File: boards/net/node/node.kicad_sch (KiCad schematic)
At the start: 0 parts

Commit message: net/node: RP2040 sensor-net node schematic with pogo programming pads and sensor variants
Proof-of-concept cell for a tiled sensor net: RP2040, W25Q16, 12 MHz crystal, ME6211 LDO,
four JST-XH neighbour links (5 V, single-wire open-drain UART, GND), WS2812B-2020 LED behind
a diode drop, buzzer driver, and a sensor port. No USB connector: J6 is a 2x4 pogo pad array
carrying SWD, USB D+/D-, RUN, BOOT and 5 V. Sensor options are KiCad 10 design variants in
one schematic: default VL53L0X ToF, "vib" SW-18010P spring switch, "bare" header only.
Schematic generated by generate/schematic.py; ERC clean; PCB not laid out yet.

schgen: local net labels, dnp, in_pos_files, per-variant overrides, prop_rot.
lib: SW-18010P vibration switch footprint.
CLAUDE.md: variant file syntax, label/property text notes, per-variant jobset idea.

Co-Authored-By: Claude Fable 5.1 <noreply@anthropic.com>
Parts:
- added BZ1: Buzzer 5V, Buzzer_Beeper:Buzzer_12x9.5RM7.6, symbol Device:Buzzer
- added C1, C2: 27p, Capacitor_SMD:C_0603_1608Metric, symbol Device:C
- added C10, C14, C15, C16, C19, C20, C22, C3, C4, C5, C6, C7, C8, C9: 100n, Capacitor_SMD:C_0603_1608Metric, symbol Device:C
- added C11, C13: 1u, Capacitor_SMD:C_0603_1608Metric, symbol Device:C
- added C12, C17, C18: 10u, Capacitor_SMD:C_0603_1608Metric, symbol Device:C
- added C21: 4u7, Capacitor_SMD:C_0603_1608Metric, symbol Device:C
- added D1, D3: 1N4148W, Diode_SMD:D_SOD-123, symbol Device:D
- added D2: WS2812B-2020, LED_SMD:LED_WS2812B-2020_PLCC4_2.0x2.0mm, symbol LED:WS2812B-2020
- added H1, H2, H3, H4: M2, MountingHole:MountingHole_2.2mm_M2, symbol Mechanical:MountingHole
- added J1: N, Connector_JST:JST_XH_B3B-XH-A_1x03_P2.50mm_Vertical, symbol Connector_Generic:Conn_01x03
- added J2: E, Connector_JST:JST_XH_B3B-XH-A_1x03_P2.50mm_Vertical, symbol Connector_Generic:Conn_01x03
- added J3: S, Connector_JST:JST_XH_B3B-XH-A_1x03_P2.50mm_Vertical, symbol Connector_Generic:Conn_01x03
- added J4: W, Connector_JST:JST_XH_B3B-XH-A_1x03_P2.50mm_Vertical, symbol Connector_Generic:Conn_01x03
- added J5: SENSOR, Connector_PinHeader_2.54mm:PinHeader_1x07_P2.54mm_Vertical, symbol Connector_Generic:Conn_01x07
- added J6: PROG, Connector_PinHeader_2.54mm:PinHeader_2x04_P2.54mm_Vertical_SMD, symbol Connector_Generic:Conn_02x04_Odd_Even
- added Q1: 2N7002, Package_TO_SOT_SMD:SOT-23, symbol Transistor_FET:2N7002
- added R1, R17: 1k, Resistor_SMD:R_0603_1608Metric, symbol Device:R
- added R10, R12, R14, R4, R5, R8: 4k7, Resistor_SMD:R_0603_1608Metric, symbol Device:R
- added R11, R13, R7, R9: 100, Resistor_SMD:R_0603_1608Metric, symbol Device:R
- added R15, R16: 27, Resistor_SMD:R_0603_1608Metric, symbol Device:R
- added R18: 100k, Resistor_SMD:R_0603_1608Metric, symbol Device:R
- added R2, R3, R6: 10k, Resistor_SMD:R_0603_1608Metric, symbol Device:R
- added SW1: SW-18010P, boards:SW-18010P, symbol Switch:SW_SPST
- added U1: RP2040, Package_DFN_QFN:QFN-56-1EP_7x7mm_P0.4mm_EP3.2x3.2mm, symbol MCU_RaspberryPi:RP2040
- added U2: W25Q16JVSSIQ, Package_SO:SOIC-8_5.3x5.3mm_P1.27mm, symbol Memory_Flash:W25Q16JVSS
- added U3: VL53L0CXV0DH/1, OptoDevice:ST_VL53L0X, symbol Sensor_Distance:VL53L0CXV0DH1
- added U4: ME6211C33M5G, Package_TO_SOT_SMD:SOT-23-5, symbol Regulator_Linear:ME6211C33M5
- added Y1: 12MHz, Crystal:Crystal_SMD_3225-4Pin_3.2x2.5mm, symbol Device:Crystal_GND24
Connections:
- new net: C2.2, R1.1, Y1.3
- new net: R1.2, U1.21 (XOUT)
- new net: J3.2 (Pin_2), R11.2
- new net: Q1.1 (G), R17.2, R18.1
- new net: BZ1.2 (-), D3.2 (A), Q1.3 (D)
- new net: C1.2, U1.20 (XIN), Y1.1
- new net: J1.2 (Pin_2), R7.2
- new net: J2.2 (Pin_2), R9.2
- new net: J6.1 (Pin_1), R15.1
- new net: J4.2 (Pin_2), R13.2
- new net: J6.3 (Pin_3), R16.1
- new net +3V3: C10.1, C11.1, C12.1, C16.1, C18.1, C20.1, C21.1, C3.1, C4.1, C5.1, C6.1, C7.1, C8.1, C9.1, J5.2 (Pin_2), R10.1, R12.1, R14.1, R2.1, R3.1, R4.1, R5.1, R6.1, R8.1, U1.1 (IOVDD), U1.10 (IOVDD), U1.22 (IOVDD), U1.33 (IOVDD), U1.42 (IOVDD), U1.43 (ADC_AVDD), U1.44 (VREG_VIN), U1.48 (USB_VDD), U1.49 (IOVDD), U2.8 (VCC), U3.1 (AVDDVCSEL), U3.11 (AVDD), U4.5 (V_{OUT})
- new net +5V: BZ1.1 (+), C17.1, D1.2 (A), D3.1 (K), J1.1 (Pin_1), J2.1 (Pin_1), J3.1 (Pin_1), J4.1 (Pin_1), J5.1 (Pin_1), J6.7 (Pin_7), U4.1 (V_{IN}), U4.3 (CE)
- new net BUZZ: R17.1, U1.7 (GPIO5)
- new net DVDD: C13.1, C14.1, C15.1, U1.23 (DVDD), U1.45 (VREG_VOUT), U1.50 (DVDD)
- new net GND: C1.1, C10.2, C11.2, C12.2, C13.2, C14.2, C15.2, C16.2, C17.2, C18.2, C19.2, C2.1, C20.2, C21.2, C22.2, C3.2, C4.2, C5.2, C6.2, C7.2, C8.2, C9.2, D2.2 (VSS), J1.3 (Pin_3), J2.3 (Pin_3), J3.3 (Pin_3), J4.3 (Pin_3), J5.7 (Pin_7), J6.5 (Pin_5), Q1.2 (S), R18.2, SW1.1 (A), U1.19 (TESTEN), U1.57 (GND), U2.4 (GND), U3.12 (GND), U3.2 (AVSSVCSEL), U3.3 (GND), U3.4 (GND), U3.6 (GND), U4.2 (V_{SS}), Y1.2 (G), Y1.4 (G)
- new net LED_DIN: D2.3 (DIN), U1.6 (GPIO4)
- new net LED_VDD: C19.1, D1.1 (K), D2.4 (VDD)
- new net LINK_E: R10.2, R9.1, U1.3 (GPIO1)
- new net LINK_N: R7.1, R8.2, U1.2 (GPIO0)
- new net LINK_S: R11.1, R12.2, U1.4 (GPIO2)
- new net LINK_W: R13.1, R14.2, U1.5 (GPIO3)
- new net QSPI_SCLK: U1.52 (QSPI_SCLK), U2.6 (CLK)
- new net QSPI_SD0: U1.53 (QSPI_SD0), U2.5 (DI/IO_{0})
- new net QSPI_SD1: U1.55 (QSPI_SD1), U2.2 (DO/IO_{1})
- new net QSPI_SD2: U1.54 (QSPI_SD2), U2.3 (~{WP}/IO_{2})
- new net QSPI_SD3: U1.51 (QSPI_SD3), U2.7 (~{HOLD}/~{RESET}/IO_{3})
- new net QSPI_SS: J6.8 (Pin_8), R3.2, U1.56 (~{QSPI_SS}), U2.1 (~{CS})
- new net RUN: J6.6 (Pin_6), R2.2, U1.26 (RUN)
- new net SCL: J5.5 (Pin_5), R5.2, U1.12 (GPIO9), U3.10 (SCL)
- new net SDA: J5.4 (Pin_4), R4.2, U1.11 (GPIO8), U3.9 (SDA)
- new net SENS_AIN: J5.6 (Pin_6), U1.38 (GPIO26/ADC0)
- new net SENS_INT: C22.1, J5.3 (Pin_3), R6.2, SW1.2 (B), U1.8 (GPIO6), U3.7 (GPIO1)
- new net SENS_XSHUT: U1.9 (GPIO7), U3.5 (XSHUT)
- new net SWCLK: J6.4 (Pin_4), U1.24 (SWCLK)
- new net SWDIO: J6.2 (Pin_2), U1.25 (SWDIO)
- new net USB_DM: R16.2, U1.46 (USB_DM)
- new net USB_DP: R15.2, U1.47 (USB_DP)
- no-connect marks 0 -> 22
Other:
- note added: "5 V comes in over the link connectors; any node can also be fed from the programming jig."
- note added: "D1 drops the LED supply to ~4.3 V so 3.3 V logic meets the WS2812B VIH (0.7 VDD)."
- note added: "J6: 2x4 pogo pads (2.54 mm), nothing fitted. SWD, or USB via 27R with BOOT grounding QSPI_SS."
- note added: "Neighbour links: 5 V, single-wire half-duplex UART (open drain, 4k7 pull-up), GND. Straight 3-wire cable, no crossover."
- note added: "Pull-ups: RUN, QSPI_SS (boot), I2C, sensor INT (open-drain GPIO1 / switch)."
- note added: "RP2040 decoupling: one 100 nF per IOVDD pin (6), USB_VDD, ADC_AVDD; 1 uF on VREG_VIN; 10 uF bulk. DVDD: 1 uF + 2 x 100 nF."
- note added: "Sensor port. J5 takes off-board modules (LD2410, AM312 PIR, I2C breakouts). U3 = default variant, SW1 = "vib" variant, "bare" = header only."
- note added: "debounce"
- title: node -> Net node: RP2040, 4 neighbour links, RGB LED, buzzer, sensor port

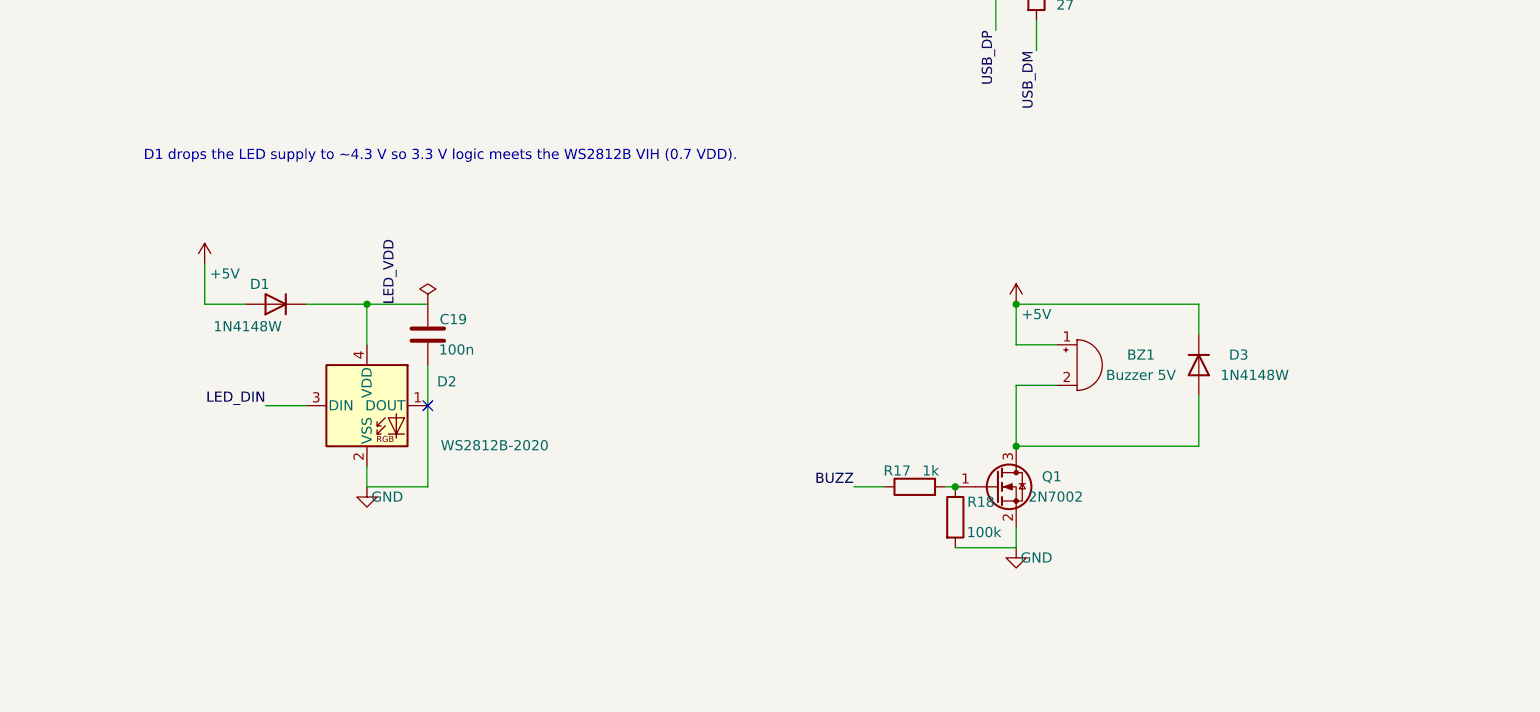
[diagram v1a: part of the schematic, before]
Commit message: net/node: second WS2812B-2020 (D4, DNP) chained on D2 for a brighter node
Regenerated schematic; C19 moved to the rail end, buzzer block shifted right.
ERC/DRC clean, D4 excluded from all three variant BOMs.

Co-Authored-By: Claude Fable 5.1 <noreply@anthropic.com>
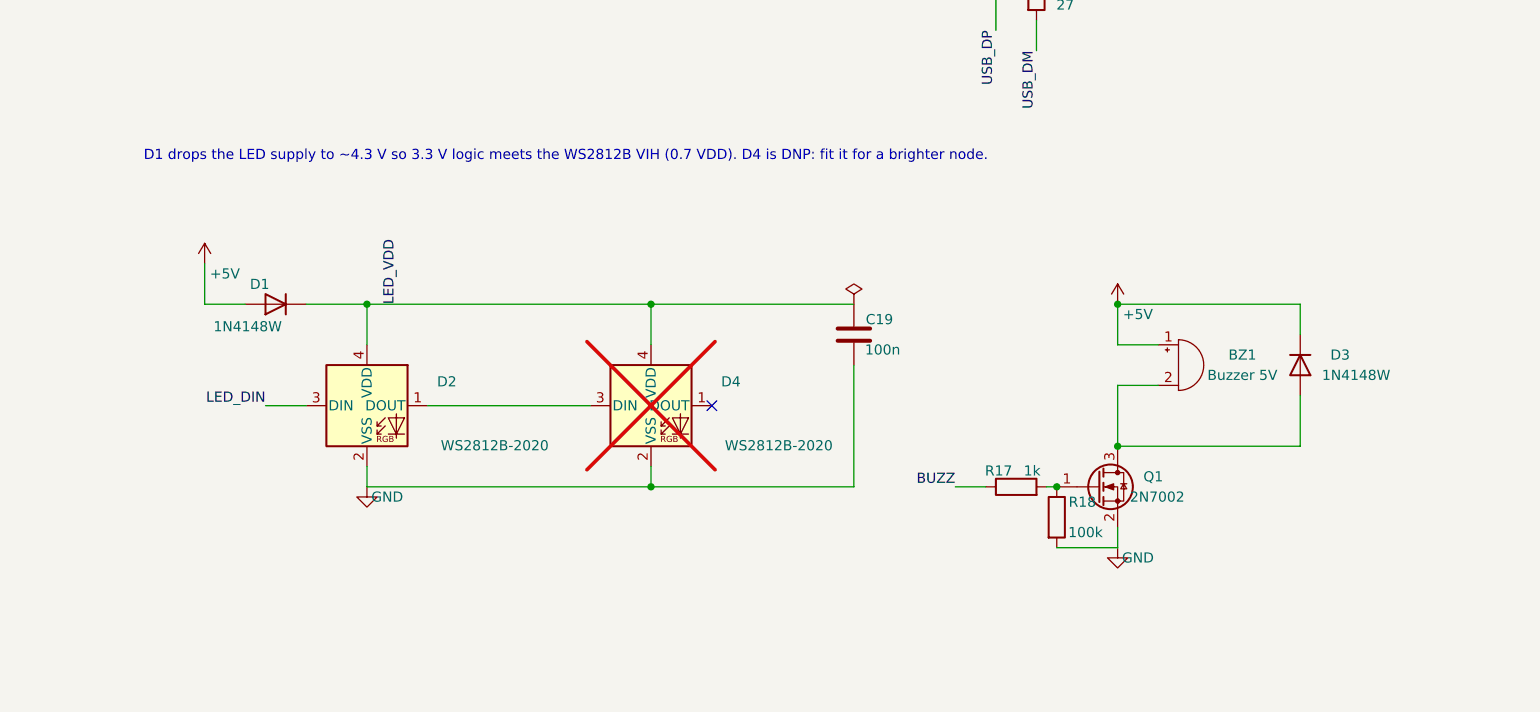
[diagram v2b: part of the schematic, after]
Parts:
- added D4: WS2812B-2020, LED_SMD:LED_WS2812B-2020_PLCC4_2.0x2.0mm, symbol LED:WS2812B-2020
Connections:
- net GND: now also D4.2 (VSS)
- net LED_VDD: now also D4.4 (VDD)
- net at D2.1 (DOUT): now also D4.3 (DIN)
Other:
- note added: "D1 drops the LED supply to ~4.3 V so 3.3 V logic meets the WS2812B VIH (0.7 VDD). D4 is DNP: fit it for a brighter node."
- note removed: "D1 drops the LED supply to ~4.3 V so 3.3 V logic meets the WS2812B VIH (0.7 VDD)."

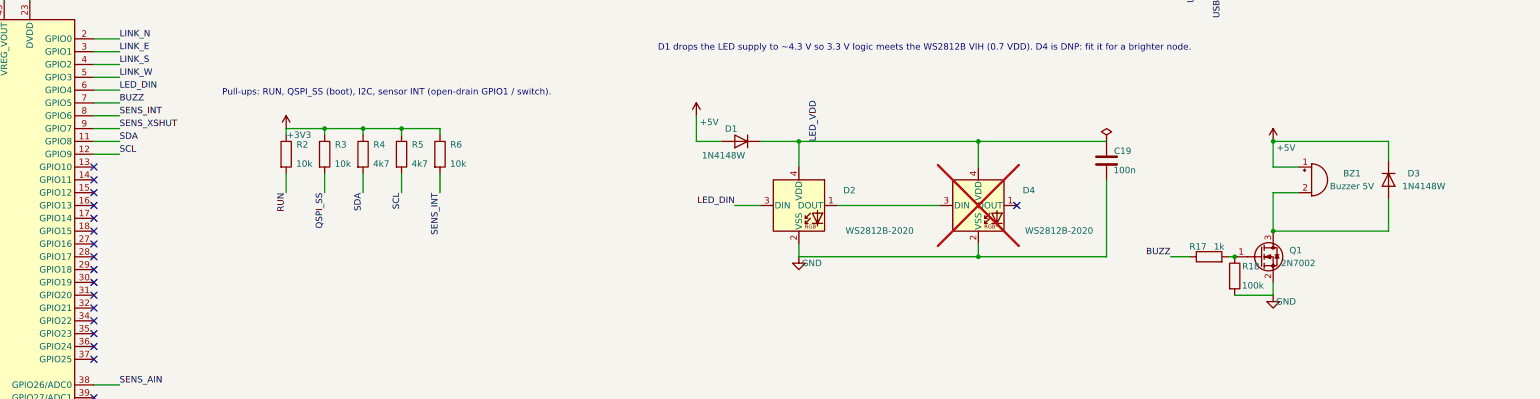
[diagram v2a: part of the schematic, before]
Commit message: net/node: drop the buzzer; pcbgen: idempotent inner layers, attr-less footprints keep flags, board-side variants
- pcbgen: InN.Cu layers are rebuilt from scratch (a generator reading its own output
  no longer accumulates copies); footprints without an attr clause still get dnp /
  exclude flags; per-variant dnp/exclude overrides from the netlist are written as
  KiCad 10 (variants ...) on the board and (variant ...) on each footprint, so
  `pcb export pos --variant` now agrees with the BOM. Tests cover all three.
- net/node: BZ1/Q1/R17/R18/D3 removed (largest part after the connectors, and a 5 V
  budget problem next to the LEDs); GPIO5 is a no-connect. ERC clean. README: buzzer
  decision, jig row spacing (5.05 mm), D4 two-pixel note, LCSC list.

Co-Authored-By: Claude Fable 5.1 <noreply@anthropic.com>
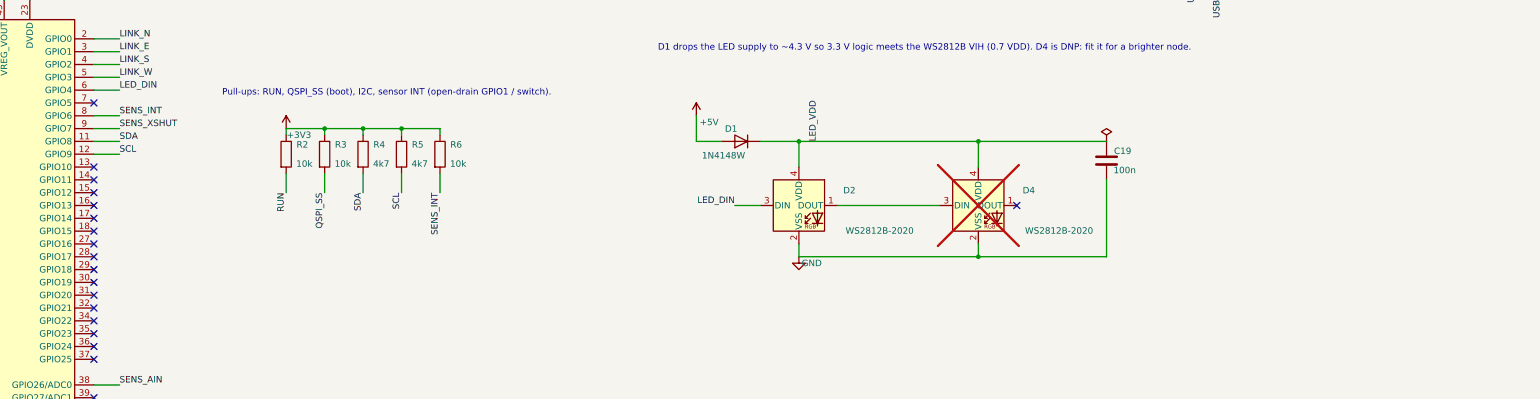
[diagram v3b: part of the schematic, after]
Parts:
- removed BZ1: Buzzer 5V, Buzzer_Beeper:Buzzer_12x9.5RM7.6, symbol Device:Buzzer
- removed D3: 1N4148W, Diode_SMD:D_SOD-123, symbol Device:D
- removed Q1: 2N7002, Package_TO_SOT_SMD:SOT-23, symbol Transistor_FET:2N7002
- removed R17: 1k, Resistor_SMD:R_0603_1608Metric, symbol Device:R
- removed R18: 100k, Resistor_SMD:R_0603_1608Metric, symbol Device:R
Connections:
- net BUZZ: no longer names the net of U1.7 (GPIO5)
- no-connect marks 22 -> 23
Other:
- title: Net node: RP2040, 4 neighbour links, RGB LED, buzzer, sensor port -> Net node: RP2040, 4 neighbour links, RGB LED, sensor port

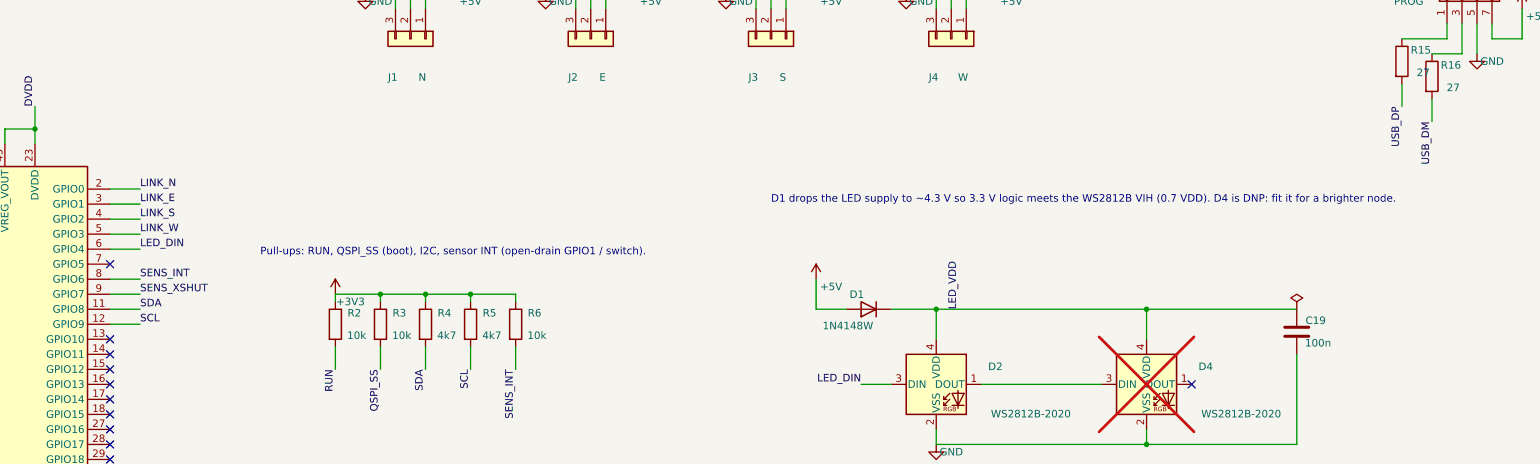
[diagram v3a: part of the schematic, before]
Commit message: net/node: place and route the board (DRC clean); pcbgen: solid_pads, zone thermals, empty fields
- Sensor GPIOs moved: XSHUT GPIO7->GPIO5, SDA/SCL GPIO8/9 -> GPIO10/11 (I2C1) so IOVDD
  pin 10's neighbours stay unrouted and it can via to the plane; J6 USB pins swapped
  (1 = DM, 3 = DP) so the traces do not cross. Schematic regenerated, ERC clean.
- pcb.py: U1 at (14, 13), 4 layers, every net routed: up-left SWD/crystal fan onto
  1.2 mm rows, down-right GPIO fan onto 0.7 mm columns, QSPI around the flash, west
  B.Cu lanes ending in vias inside the pogo pads, 0.8 mm 5 V ring notched around three
  M2 keepouts and open at the top-left corner, planes on In1/In2. make check: 0
  violations, 0 unconnected, 0 parity issues (two dangling-end warnings = the open ring).
- pcbgen: solid_pads= (J4 pin 3), zone thermal_gap/thermal_bridge, empty schematic fields
  written as empty properties (parity), ref_pos documented as rotating with the part.
- READMEs: PCB section rewritten for the routed board, resume path, generate commands.
  CLAUDE.md: 0.4 mm pitch escape/via rules, pad offsets, flatpak KiCad setup.

Co-Authored-By: Claude Fable 5.1 <noreply@anthropic.com>
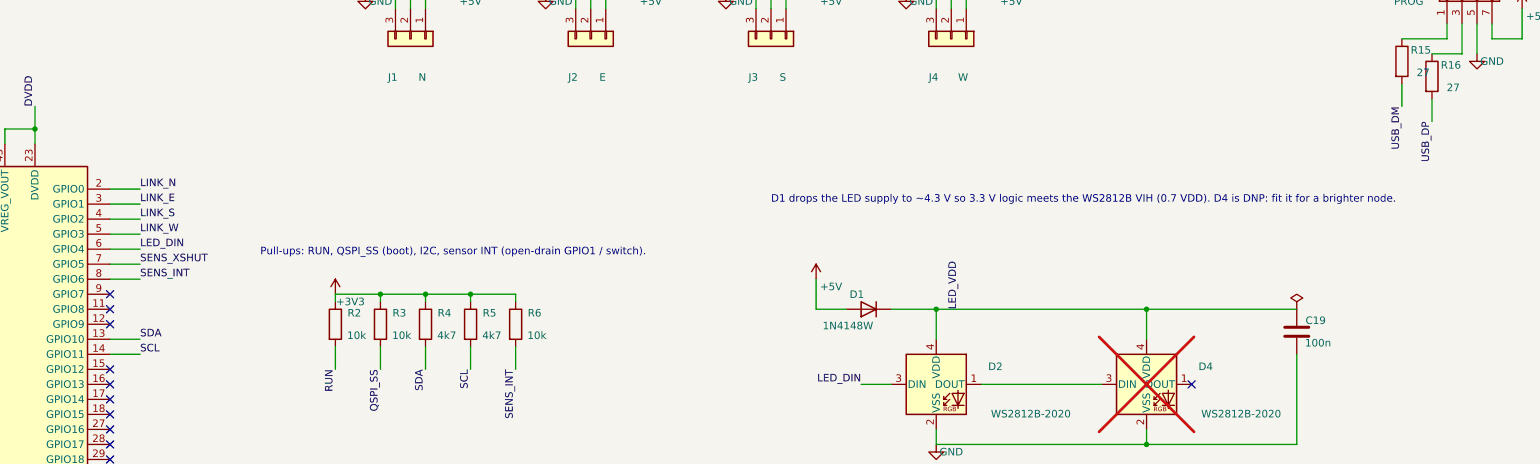
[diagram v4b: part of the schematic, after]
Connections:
- net SCL: now also U1.14 (GPIO11); no longer U1.12 (GPIO9)
- net SDA: now also U1.13 (GPIO10); no longer U1.11 (GPIO8)
- net SENS_XSHUT: now also U1.7 (GPIO5); no longer U1.9 (GPIO7)
- net USB_DM: now also R15.2; no longer R16.2
- net USB_DP: now also R16.2; no longer R15.2
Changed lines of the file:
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@@
 	(wire
 		(pts
-			(xy 139.7 104.14)
-			(xy 144.78 104.14)
+			(xy 139.7 101.6)
+			(xy 144.78 101.6)
 		)
 		(stroke
@@
 		)
 	)
-	(label "SENS_INT"
-		(at 144.78 104.14 0)
+	(label "SENS_XSHUT"
+		(at 144.78 101.6 0)
 		(effects
 			(font
@@
 	(wire
 		(pts
-			(xy 139.7 106.68)
-			(xy 144.78 106.68)
+			(xy 139.7 104.14)
+			(xy 144.78 104.14)
 		)
 		(stroke
@@
 		)
 	)
-	(label "SENS_XSHUT"
-		(at 144.78 106.68 0)
+	(label "SENS_INT"
+		(at 144.78 104.14 0)
 		(effects
 			(font
@@
 	(wire
 		(pts
-			(xy 139.7 109.22)
-			(xy 144.78 109.22)
+			(xy 139.7 114.3)
+			(xy 144.78 114.3)
 		)
 		(stroke
@@
 	)
 	(label "SDA"
-		(at 144.78 109.22 0)
+		(at 144.78 114.3 0)
 		(effects
 			(font
@@
 	(wire
 		(pts
-			(xy 139.7 111.76)
-			(xy 144.78 111.76)
+			(xy 139.7 116.84)
+			(xy 144.78 116.84)
 		)
 		(stroke
@@
 	)
 	(label "SCL"
-		(at 144.78 111.76 0)
+		(at 144.78 116.84 0)
 		(effects
 			(font
@@
 	)
 	(no_connect
-		(at 139.7 101.6)
+		(at 139.7 106.68)
 	)
 	(no_connect
-		(at 139.7 114.3)
+		(at 139.7 109.22)
 	)
 	(no_connect
-		(at 139.7 116.84)
+		(at 139.7 111.76)
 	)
 	(no_connect
@@
 		)
 	)
-	(label "USB_DP"
+	(label "USB_DM"
 		(at 358.14 74.93 270)
 		(effects
@@
 		)
 	)
-	(label "USB_DM"
+	(label "USB_DP"
 		(at 363.22 77.47 270)
 		(effects

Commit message: net/node: piezo sounder BZ1 (Murata PKMCS0909E, 9 mm SMD) on GPIO12/13 via 100 R, antiphase drive
Schematic only: BZ1 + R17/R18, ERC clean, netlist regenerated; placement and routing follow.
README: decision, GPIO map, refdes table.

Co-Authored-By: Claude Fable 5.1 <noreply@anthropic.com>
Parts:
- added BZ1: PKMCS0909E4000-R1, Buzzer_Beeper:Buzzer_Murata_PKMCS0909E, symbol Device:Buzzer
- added R17, R18: 100, Resistor_SMD:R_0603_1608Metric, symbol Device:R
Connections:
- net BUZZ_A: now reaches U1.15 (GPIO12)
- net BUZZ_A: now also R17.1
- net BUZZ_B: now reaches U1.16 (GPIO13)
- net BUZZ_B: now also R18.1
- new net: BZ1.1 (+), R17.2
- new net: BZ1.2 (-), R18.2
- no-connect marks 23 -> 21
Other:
- note added: "Piezo element, not a self-oscillating buzzer: pitch = drive frequency (PWM/PIO). Two GPIOs in antiphase give 6.6 Vpp; one GPIO and the other held low gives half."
- title: Net node: RP2040, 4 neighbour links, RGB LED, sensor port -> Net node: RP2040, 4 neighbour links, RGB LED, piezo, sensor port
